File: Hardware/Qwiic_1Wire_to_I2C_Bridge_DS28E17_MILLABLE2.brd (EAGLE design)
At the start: 45.7 x 27.9 mm, 20 parts, among them J1 RJ45, J2 RJ45, J3 RJ11, J4 RJ11

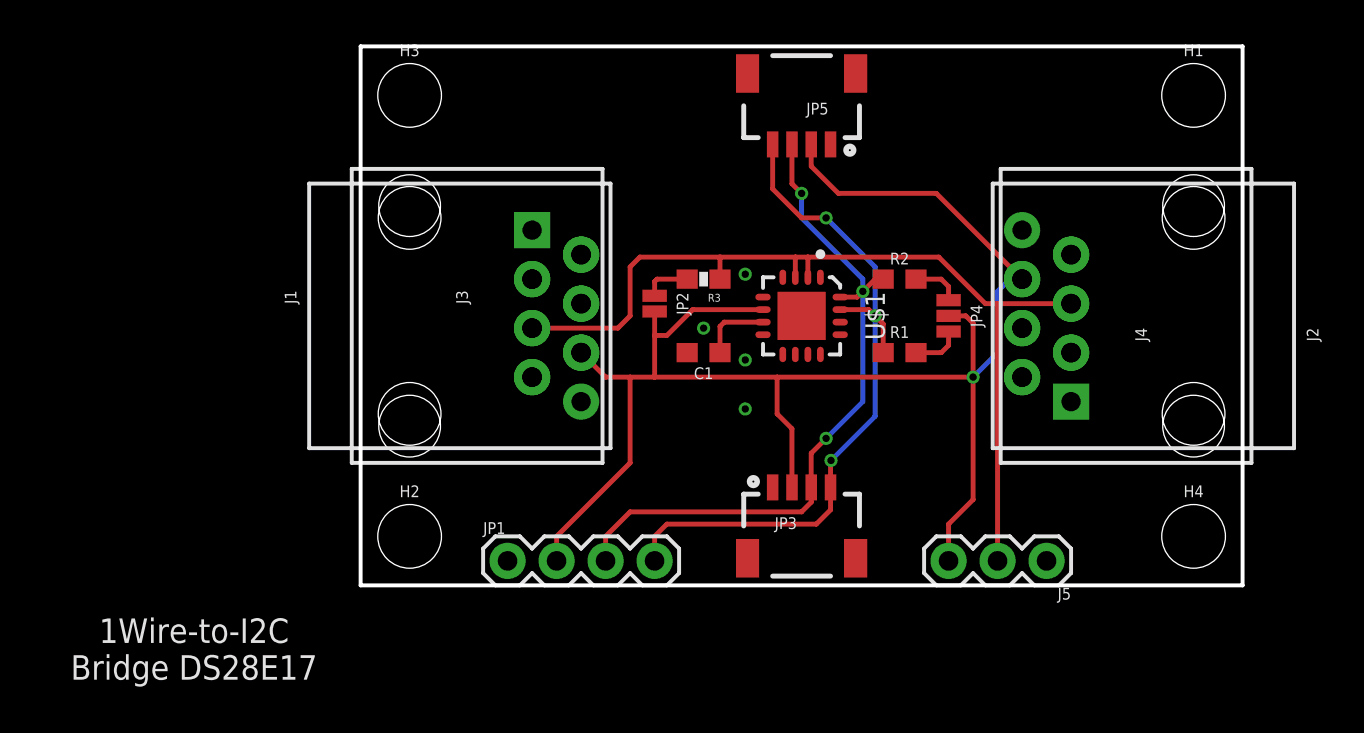
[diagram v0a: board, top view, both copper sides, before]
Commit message: Routed more on production layout
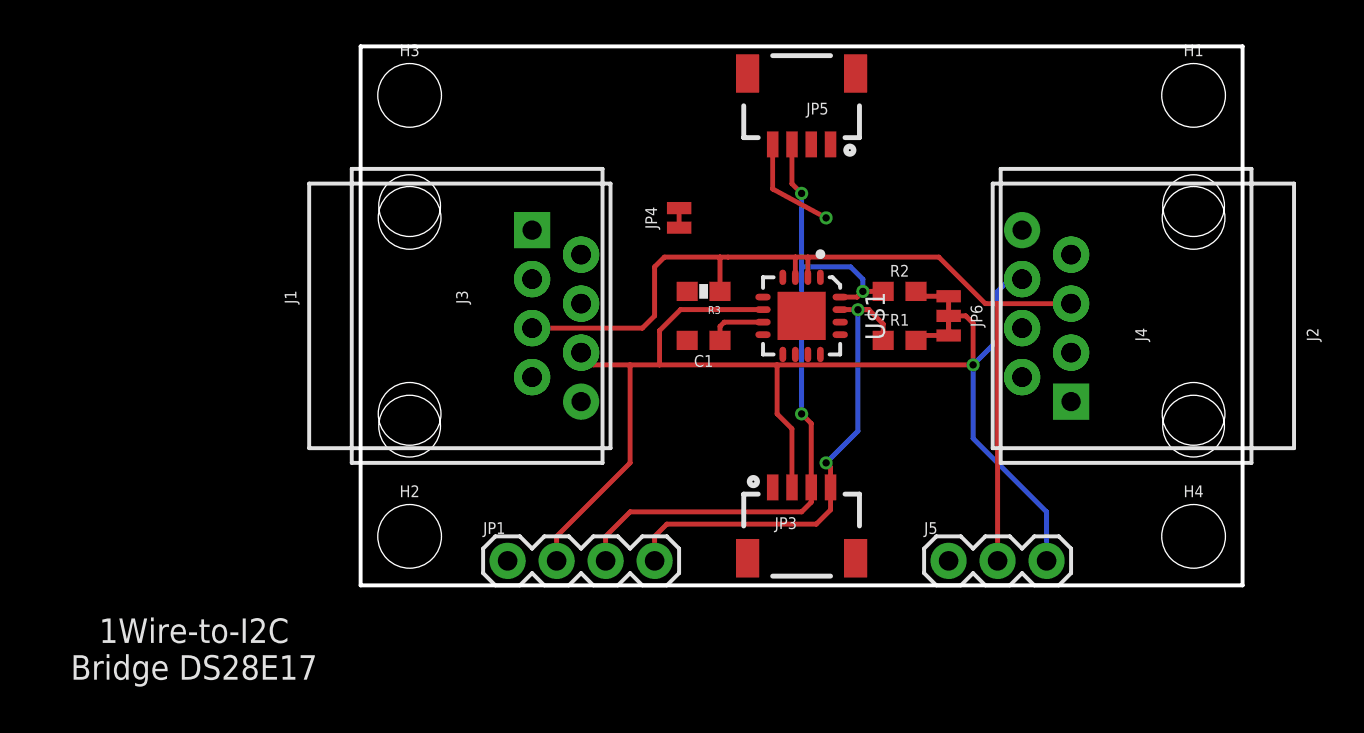
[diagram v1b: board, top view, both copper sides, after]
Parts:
- removed JP2: (no value), SparkFun-Jumpers:SMT-JUMPER_2_NO_NO-SILK
- added JP6: (no value), SparkFun-Jumpers:SMT-JUMPER_3_2-NC_TRACE_NO-SILK
- JP4: device SparkFun-Jumpers:SMT-JUMPER_3_NO_NO-SILK -> SparkFun-Jumpers:SMT-JUMPER_2_NC_TRACE_NO-SILK
- moved JP4 14.9 mm to (16.5, 19.1), turned to 90 degrees
- moved J5 5.08 mm to (30.5, 1.27), turned to 0 degrees
- moved C1 0.63 mm to (17.8, 12.7)
- moved R1 0.63 mm to (27.9, 12.7)
- moved R2 0.63 mm to (27.9, 15.2)
- moved R3 0.63 mm to (17.8, 15.2)
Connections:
- net 3.3V: now also JP6.2; no longer JP2.2
- net N$2: now also JP4.1; no longer JP2.1
- net N$3: now also JP6.1; no longer JP4.1
- net N$4: now also JP6.3; no longer JP4.3
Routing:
- net 3.3V: track 82.8 -> 68.8 mm
- net SCL: track 37.8 -> 31.5 mm
- net N$2: track 2.48 -> 0.00 mm
- net SDA: track 36.5 -> 38.1 mm
- net N$3: track 2.56 -> 1.80 mm
- net N$4: track 2.56 -> 1.80 mm
- net N$1: track 3.68 -> 3.04 mm
- net IO: track 48.5 -> 49.2 mm
- removed copper zone on layer 1, net GND
- removed copper zone on layer 16, net GND

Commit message: MIllable version 2
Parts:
- removed JP1: (no value), SparkX:1X04
- removed JP4: (no value), SparkFun-Jumpers:SMT-JUMPER_2_NC_TRACE_NO-SILK
- removed JP5: (no value), SparkX:1X04_1MM_RA
- removed JP6: (no value), SparkFun-Jumpers:SMT-JUMPER_3_2-NC_TRACE_NO-SILK
- added JP2: (no value), SparkFun-Jumpers:SMT-JUMPER_2_NO_NO-SILK
- added JP7: (no value), SparkFun-Jumpers:SMT-JUMPER_3_NO_NO-SILK
- added TP1, TP2: TEST-POINT3X4, SparkFun-Connectors:PAD.03X.04
- moved J5 5.08 mm to (35.6, 1.27), turned to 180 degrees
- flipped J1 to the bottom, turned to 90 degrees
- flipped J2 to the bottom, turned to 270 degrees
- flipped J3 to the bottom, turned to 90 degrees
- flipped J4 to the bottom, turned to 270 degrees
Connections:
- new net N$5: JP3.4, TP1.P$1
- new net N$6: JP3.3, TP2.P$1
- net 3.3V: now also JP2.2, JP7.2; no longer JP1.2, JP4.2, JP5.2, JP6.2
- net GND: no longer JP1.1, JP5.1
- net N$2: now also JP2.1; no longer JP4.1
- net N$3: now also JP7.1; no longer JP6.1
- net N$4: now also JP7.3; no longer JP6.3
- net SCL: no longer JP1.4, JP3.4, JP5.4
- net SDA: no longer JP1.3, JP3.3, JP5.3
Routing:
- net SDA: track 38.1 -> 2.35 mm, vias 3 -> 0
- net IO: track 49.2 -> 79.9 mm
- net SCL: track 31.5 -> 3.39 mm, vias 3 -> 0
- net 3.3V: track 68.8 -> 51.2 mm, vias 1 -> 0
- net N$6: track 0.00 -> 4.13 mm
- net N$5: track 0.00 -> 2.97 mm
- net N$2: track 0.00 -> 2.40 mm
- net N$4: track 1.80 -> 2.51 mm
- net N$3: track 1.80 -> 2.51 mm
- added copper zone on layer 1, net GND
